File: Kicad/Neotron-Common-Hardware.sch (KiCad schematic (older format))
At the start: 12 parts

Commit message: Added empty SD card sheet.
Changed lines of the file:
@@
 $Descr A4 11693 8268
 encoding utf-8
-Sheet 1 9
+Sheet 1 10
 Title "Neotron Common Hardware"
 Date "2020-12-25"
@@
 NoConn ~ 4000 3250
 NoConn ~ 4000 3350
+$Sheet
+S 7000 3000 1000 1000
+U 5FEF6B08
+F0 "SD Card" 50
+F1 "sdcard.sch" 50
+$EndSheet
 $EndSCHEMATC

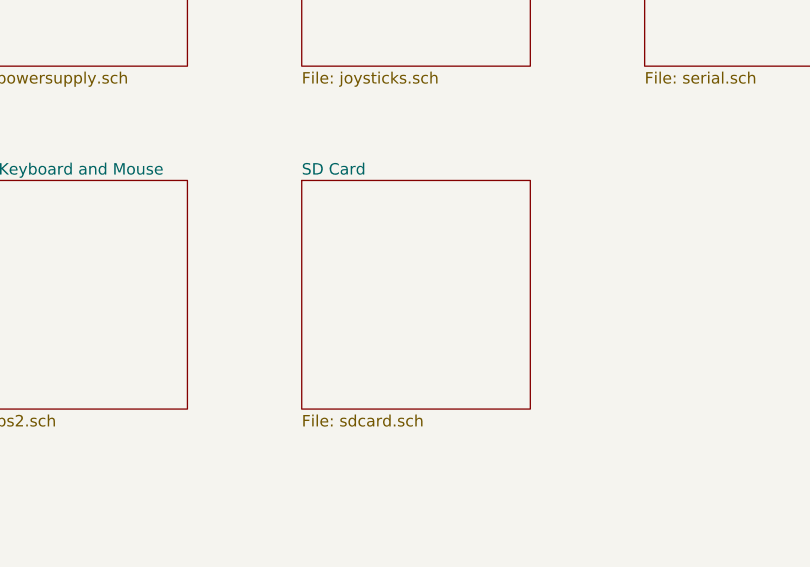
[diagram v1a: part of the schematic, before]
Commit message: Added SD card sheet.
Simple setup - 10k pullups, no ESD protection.
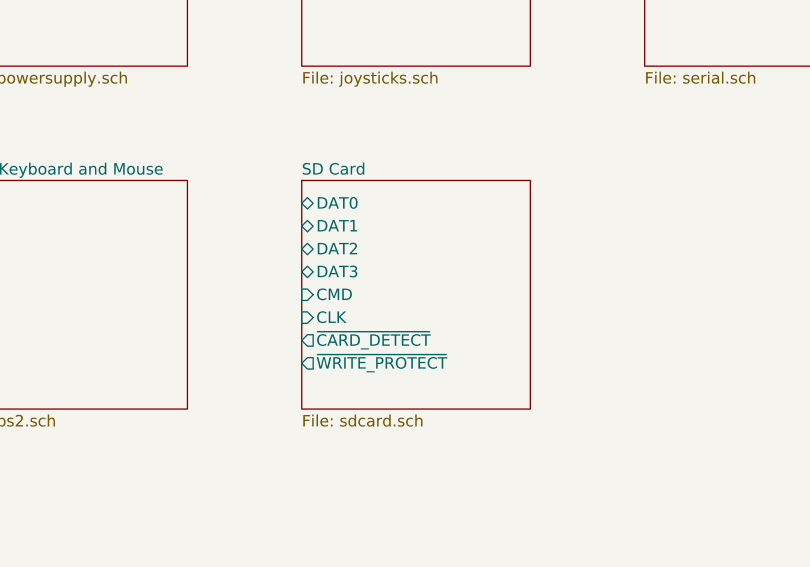
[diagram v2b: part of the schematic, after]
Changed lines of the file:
@@
 F0 "SD Card" 50
 F1 "sdcard.sch" 50
+F2 "DAT2" B L 7000 3300 50
+F3 "DAT3" B L 7000 3400 50
+F4 "CMD" I L 7000 3500 50
+F5 "CLK" I L 7000 3600 50
+F6 "DAT0" B L 7000 3100 50
+F7 "DAT1" B L 7000 3200 50
+F8 "~CARD_DETECT" O L 7000 3700 50
+F9 "~WRITE_PROTECT" O L 7000 3800 50
 $EndSheet
 $EndSCHEMATC

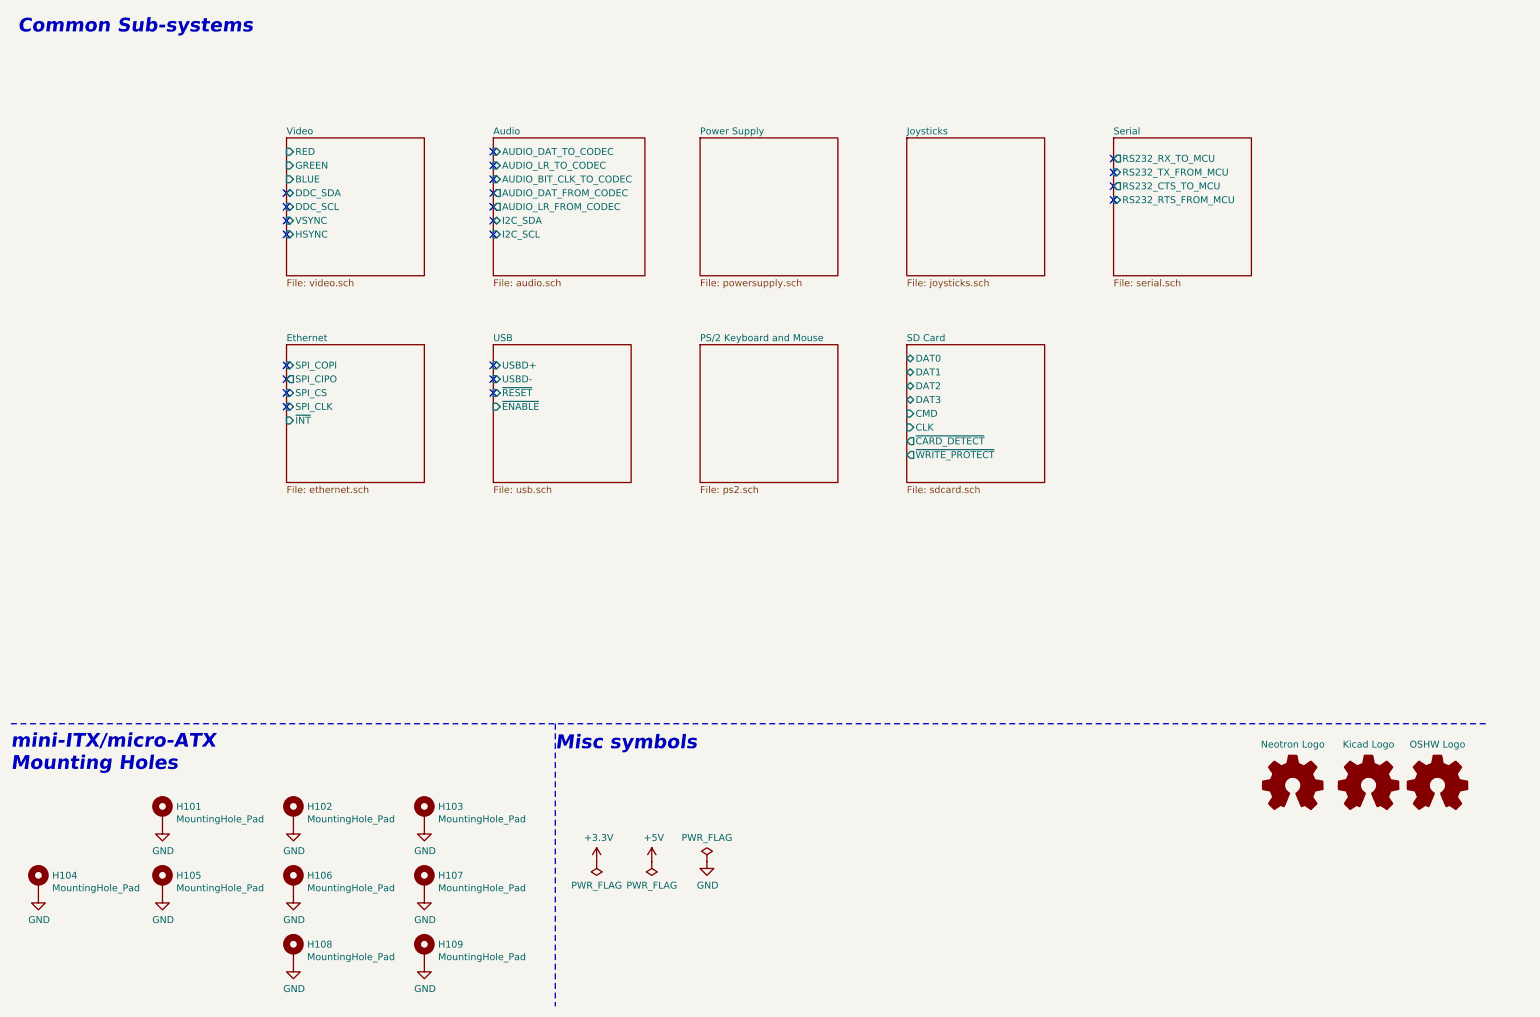
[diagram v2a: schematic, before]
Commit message: Completed PSU design.
Also changed footprint for stacked USB connector to change
shield pins from SHx to Pin 9.
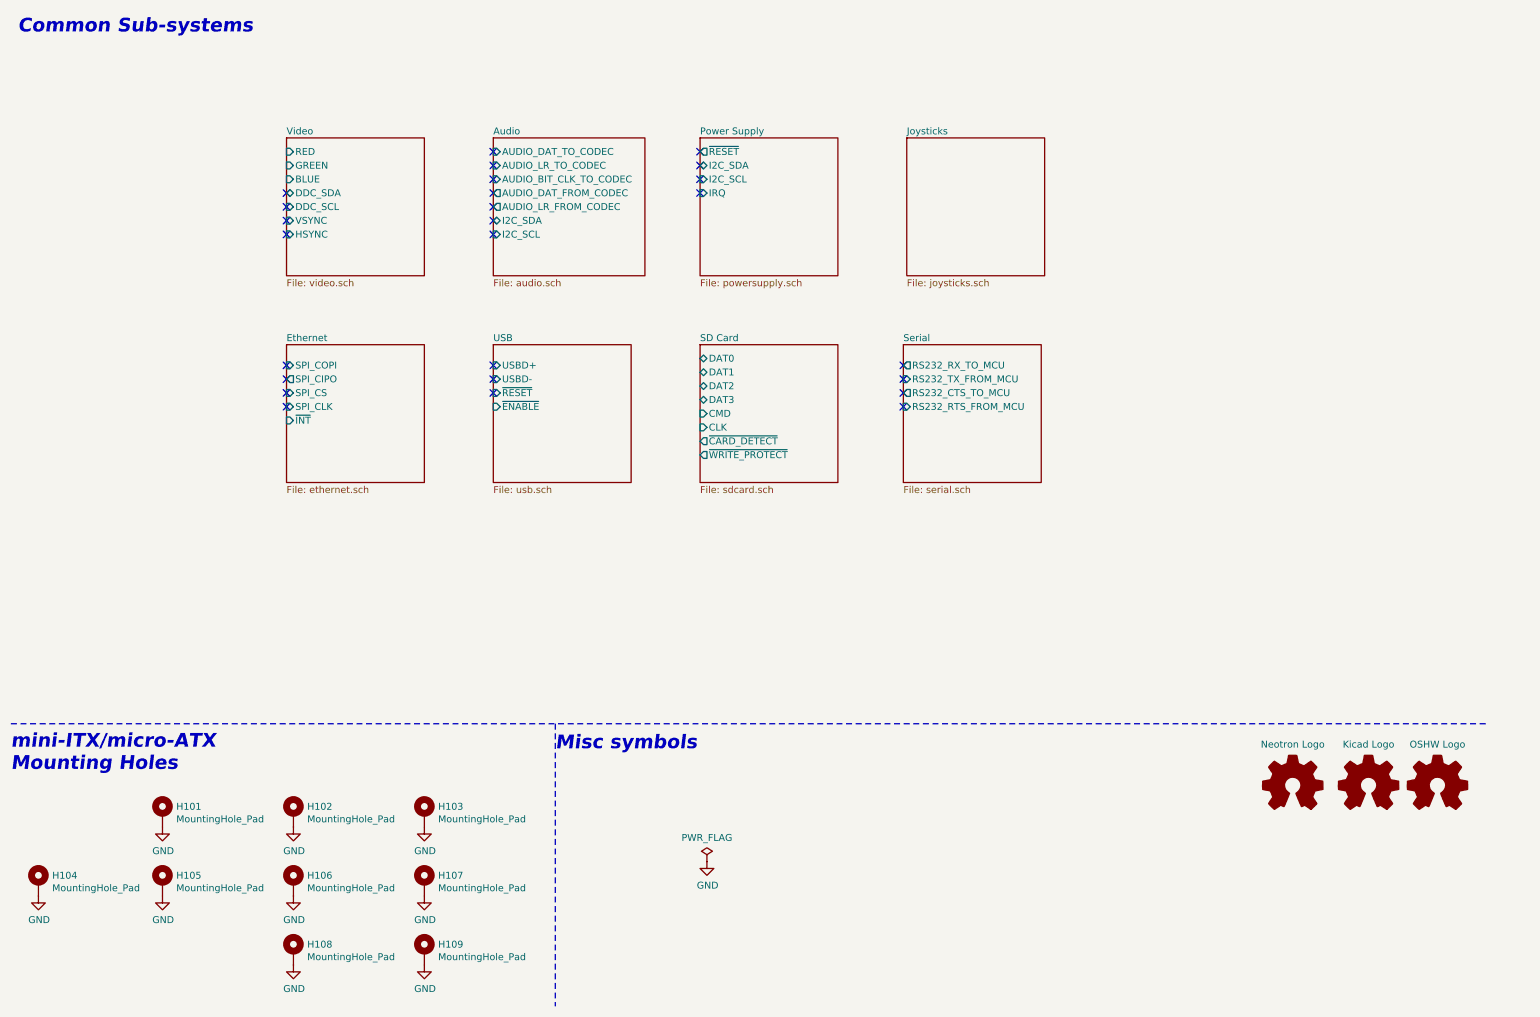
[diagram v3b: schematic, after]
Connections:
- no-connect marks 22 -> 26
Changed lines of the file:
@@
 $Descr A4 11693 8268
 encoding utf-8
-Sheet 1 10
+Sheet 1 9
 Title "Neotron Common Hardware"
-Date "2020-12-25"
+Date "2020-12-26"
 Rev "[Uncontrolled]"
 Comp "https://neotron-compute.github.io/"
@@
 F0 "Power Supply" 50
 F1 "powersupply.sch" 50
-$EndSheet
-$Sheet
-S 5500 3000 1000 1000
-U 5FDEDE75
-F0 "PS/2 Keyboard and Mouse" 50
-F1 "ps2.sch" 50
-$EndSheet
-$Sheet
-S 8500 1500 1000 1000
+F2 "~RESET" O L 5500 1600 50
+F3 "I2C_SDA" B L 5500 1700 50
+F4 "I2C_SCL" I L 5500 1800 50
+F5 "IRQ" I L 5500 1900 50
+$EndSheet
+$Sheet
+S 6975 3000 1000 1000
 U 5FDF53DB
 F0 "Serial" 50
 F1 "serial.sch" 50
-F2 "RS232_TX_FROM_MCU" I L 8500 1750 50
-F3 "RS232_RX_TO_MCU" O L 8500 1650 50
-F4 "RS232_RTS_FROM_MCU" I L 8500 1950 50
-F5 "RS232_CTS_TO_MCU" O L 8500 1850 50
+F2 "RS232_TX_FROM_MCU" I L 6975 3250 50
+F3 "RS232_RX_TO_MCU" O L 6975 3150 50
+F4 "RS232_RTS_FROM_MCU" I L 6975 3450 50
+F5 "RS232_CTS_TO_MCU" O L 6975 3350 50
 $EndSheet
 $Sheet
@@
 F1 "joysticks.sch" 50
 $EndSheet
-$Comp
-L power:+3.3V #PWR0101
-U 1 1 60A59BC0
-P 4750 6750
-F 0 "#PWR0101" H 4750 6600 50  0001 C CNN
-F 1 "+3.3V" H 4765 6923 50  0000 C CNN
-F 2 "" H 4750 6750 50  0001 C CNN
-F 3 "" H 4750 6750 50  0001 C CNN
-	1    4750 6750
-	1    0    0    -1
-$EndComp
-$Comp
-L power:+5V #PWR0102
-U 1 1 60A5A21B
-P 5150 6750
-F 0 "#PWR0102" H 5150 6600 50  0001 C CNN
-F 1 "+5V" H 5165 6923 50  0000 C CNN
-F 2 "" H 5150 6750 50  0001 C CNN
-F 3 "" H 5150 6750 50  0001 C CNN
-	1    5150 6750
-	1    0    0    -1
-$EndComp
-$Comp
-L power:PWR_FLAG #FLG0102
-U 1 1 60A5B443
-P 5150 6750
-F 0 "#FLG0102" H 5150 6825 50  0001 C CNN
-F 1 "PWR_FLAG" H 5150 6923 50  0000 C CNN
-F 2 "" H 5150 6750 50  0001 C CNN
-F 3 "~" H 5150 6750 50  0001 C CNN
-	1    5150 6750
-	-1   0    0    1
-$EndComp
-$Comp
-L power:PWR_FLAG #FLG0101
-U 1 1 60A5BC87
-P 4750 6750
-F 0 "#FLG0101" H 4750 6825 50  0001 C CNN
-F 1 "PWR_FLAG" H 4750 6923 50  0000 C CNN
-F 2 "" H 4750 6750 50  0001 C CNN
-F 3 "~" H 4750 6750 50  0001 C CNN
-	1    4750 6750
-	-1   0    0    1
-$EndComp
 NoConn ~ 4000 1600
 NoConn ~ 4000 1700
@@
 NoConn ~ 4000 2100
 NoConn ~ 4000 2200
-NoConn ~ 8500 1650
-NoConn ~ 8500 1750
-NoConn ~ 8500 1850
-NoConn ~ 8500 1950
+NoConn ~ 6975 3150
+NoConn ~ 6975 3250
+NoConn ~ 6975 3350
+NoConn ~ 6975 3450
 NoConn ~ 2500 3250
 NoConn ~ 2500 3350
@@
 NoConn ~ 2500 2100
 NoConn ~ 2500 2200
+NoConn ~ 4000 3150
+NoConn ~ 4000 3250
+NoConn ~ 4000 3350
+$Sheet
+S 5500 3000 1000 1000
+U 5FEF6B08
+F0 "SD Card" 50
+F1 "sdcard.sch" 50
+F2 "DAT2" B L 5500 3300 50
+F3 "DAT3" B L 5500 3400 50
+F4 "CMD" I L 5500 3500 50
+F5 "CLK" I L 5500 3600 50
+F6 "DAT0" B L 5500 3100 50
+F7 "DAT1" B L 5500 3200 50
+F8 "~CARD_DETECT" O L 5500 3700 50
+F9 "~WRITE_PROTECT" O L 5500 3800 50
+$EndSheet
+$Comp
+L power:PWR_FLAG #FLG0103
+U 1 1 60A5B22E
+P 5550 6750
+F 0 "#FLG0103" H 5550 6825 50  0001 C CNN
+F 1 "PWR_FLAG" H 5550 6923 50  0000 C CNN
+F 2 "" H 5550 6750 50  0001 C CNN
+F 3 "~" H 5550 6750 50  0001 C CNN
+	1    5550 6750
+	1    0    0    -1
+$EndComp
 $Comp
 L power:GND #PWR0103
@@
 	1    0    0    -1
 $EndComp
-$Comp
-L power:PWR_FLAG #FLG0103
-U 1 1 60A5B22E
-P 5550 6750
-F 0 "#FLG0103" H 5550 6825 50  0001 C CNN
-F 1 "PWR_FLAG" H 5550 6923 50  0000 C CNN
-F 2 "" H 5550 6750 50  0001 C CNN
-F 3 "~" H 5550 6750 50  0001 C CNN
-	1    5550 6750
-	1    0    0    -1
-$EndComp
-NoConn ~ 4000 3150
-NoConn ~ 4000 3250
-NoConn ~ 4000 3350
-$Sheet
-S 7000 3000 1000 1000
-U 5FEF6B08
-F0 "SD Card" 50
-F1 "sdcard.sch" 50
-F2 "DAT2" B L 7000 3300 50
-F3 "DAT3" B L 7000 3400 50
-F4 "CMD" I L 7000 3500 50
-F5 "CLK" I L 7000 3600 50
-F6 "DAT0" B L 7000 3100 50
-F7 "DAT1" B L 7000 3200 50
-F8 "~CARD_DETECT" O L 7000 3700 50
-F9 "~WRITE_PROTECT" O L 7000 3800 50
-$EndSheet
+NoConn ~ 5500 1600
+NoConn ~ 5500 1700
+NoConn ~ 5500 1800
+NoConn ~ 5500 1900
 $EndSCHEMATC

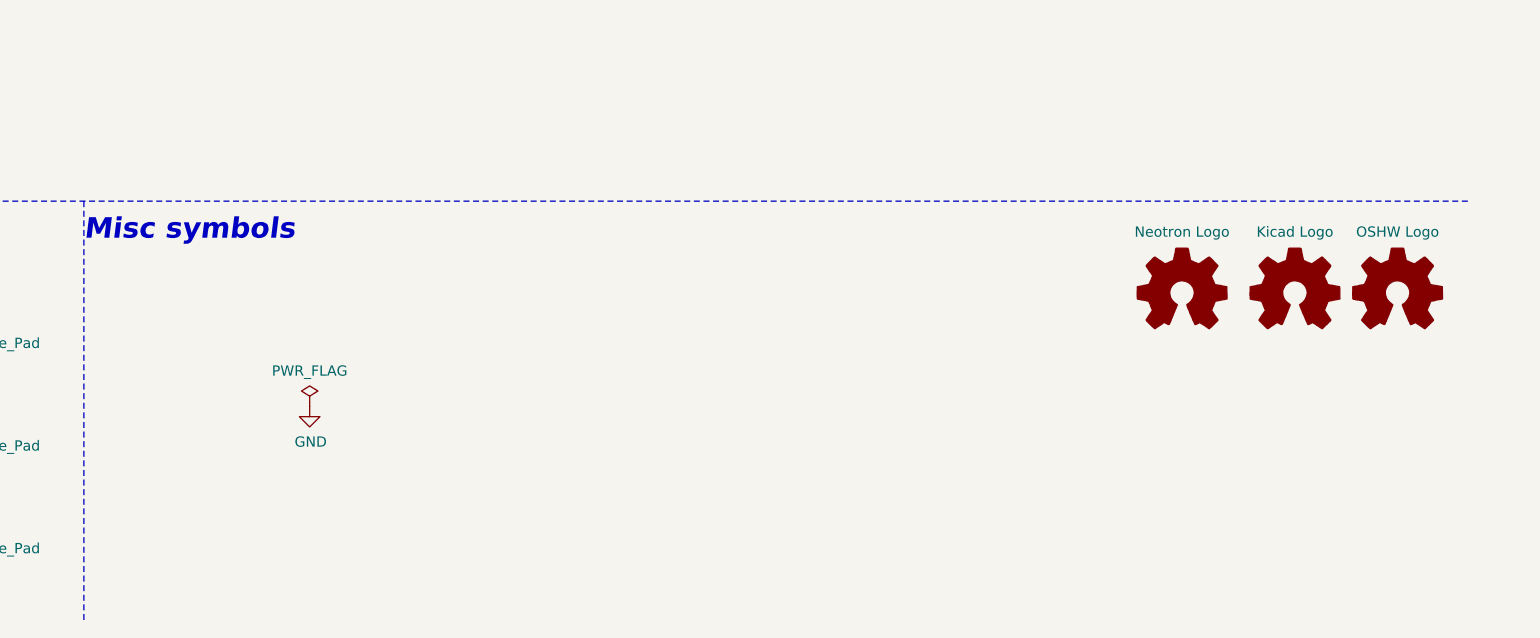
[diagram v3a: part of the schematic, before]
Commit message: Replaced NUC029 (TSSOP) with KE04 (SOIC).
Also updated the BOM with some part nos.
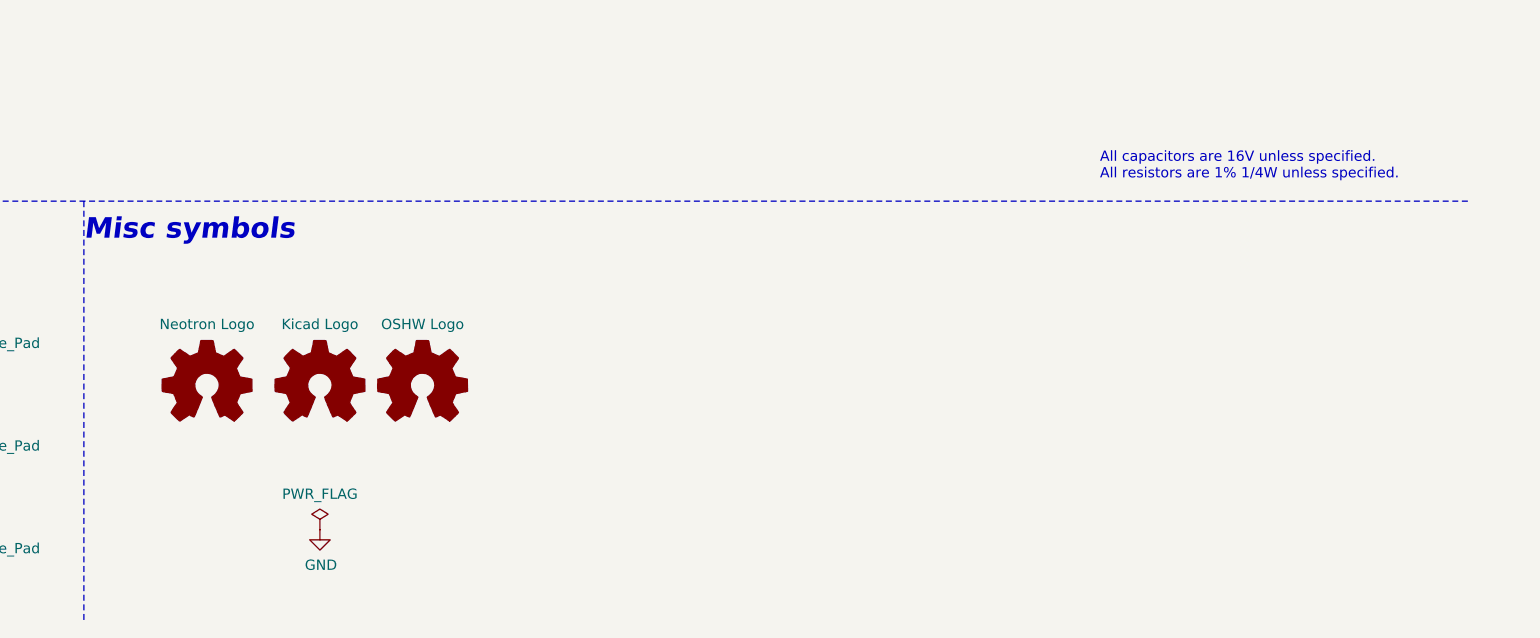
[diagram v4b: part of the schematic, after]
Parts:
- H101, H102, H103, H104, H105, H106, H107, H108, H109, LOGO101, LOGO102, LOGO103: DNP (none) -> 0
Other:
- note added: "All capacitors are 16V unless specified.\nAll resistors are 1% 1/4W unless specified."
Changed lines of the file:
@@
 F 2 "MountingHole:MountingHole_4.3mm_M4_Pad_Via" H 1600 6400 50  0001 C CNN
 F 3 "~" H 1600 6400 50  0001 C CNN
+F 4 "0" H 1600 6400 50  0001 C CNN "DNP"
 	1    1600 6400
 	1    0    0    -1
@@
 F 2 "MountingHole:MountingHole_4.3mm_M4_Pad_Via" H 1600 6900 50  0001 C CNN
 F 3 "~" H 1600 6900 50  0001 C CNN
+F 4 "0" H 1600 6900 50  0001 C CNN "DNP"
 	1    1600 6900
 	1    0    0    -1
@@
 F 2 "MountingHole:MountingHole_4.3mm_M4_Pad_Via" H 2550 6400 50  0001 C CNN
 F 3 "~" H 2550 6400 50  0001 C CNN
+F 4 "0" H 2550 6400 50  0001 C CNN "DNP"
 	1    2550 6400
 	1    0    0    -1
@@
 F 2 "MountingHole:MountingHole_4.3mm_M4_Pad_Via" H 2550 6900 50  0001 C CNN
 F 3 "~" H 2550 6900 50  0001 C CNN
+F 4 "0" H 2550 6900 50  0001 C CNN "DNP"
 	1    2550 6900
 	1    0    0    -1
@@
 F 2 "MountingHole:MountingHole_4.3mm_M4_Pad_Via" H 3500 6400 50  0001 C CNN
 F 3 "~" H 3500 6400 50  0001 C CNN
+F 4 "0" H 3500 6400 50  0001 C CNN "DNP"
 	1    3500 6400
 	1    0    0    -1
@@
 F 2 "MountingHole:MountingHole_4.3mm_M4_Pad_Via" H 2550 7400 50  0001 C CNN
 F 3 "~" H 2550 7400 50  0001 C CNN
+F 4 "0" H 2550 7400 50  0001 C CNN "DNP"
 	1    2550 7400
 	1    0    0    -1
@@
 F 2 "MountingHole:MountingHole_4.3mm_M4_Pad_Via" H 700 6900 50  0001 C CNN
 F 3 "~" H 700 6900 50  0001 C CNN
+F 4 "0" H 700 6900 50  0001 C CNN "DNP"
 	1    700  6900
 	1    0    0    -1
@@
 F 2 "MountingHole:MountingHole_4.3mm_M4_Pad_Via" H 3500 7400 50  0001 C CNN
 F 3 "~" H 3500 7400 50  0001 C CNN
+F 4 "0" H 3500 7400 50  0001 C CNN "DNP"
 	1    3500 7400
 	1    0    0    -1
@@
 F 2 "MountingHole:MountingHole_4.3mm_M4_Pad_Via" H 3500 6900 50  0001 C CNN
 F 3 "~" H 3500 6900 50  0001 C CNN
+F 4 "0" H 3500 6900 50  0001 C CNN "DNP"
 	1    3500 6900
 	1    0    0    -1
@@
 L Graphic:Logo_Open_Hardware_Small LOGO101
 U 1 1 5FE3E77B
-P 10850 6200
-F 0 "LOGO101" H 10850 6475 50  0001 C CNN
-F 1 "OSHW Logo" H 10850 6500 50  0000 C CNN
-F 2 "Symbol:OSHW-Logo_11.4x12mm_SilkScreen" H 10850 6494 50  0001 C CNN
-F 3 "~" H 10850 6200 50  0001 C CNN
-	1    10850 6200
+P 6100 6650
+F 0 "LOGO101" H 6100 6925 50  0001 C CNN
+F 1 "OSHW Logo" H 6100 6950 50  0000 C CNN
+F 2 "Symbol:OSHW-Logo_11.4x12mm_SilkScreen" H 6100 6944 50  0001 C CNN
+F 3 "~" H 6100 6650 50  0001 C CNN
+F 4 "0" H 6100 6650 50  0001 C CNN "DNP"
+	1    6100 6650
 	1    0    0    -1
 $EndComp
@@
 L Graphic:Logo_Open_Hardware_Small LOGO102
 U 1 1 5FE412EB
-P 10350 6200
-F 0 "LOGO102" H 10350 6475 50  0001 C CNN
-F 1 "Kicad Logo" H 10350 6500 50  0000 C CNN
-F 2 "Symbol:KiCad-Logo2_12mm_SilkScreen" H 10350 6494 50  0001 C CNN
-F 3 "~" H 10350 6200 50  0001 C CNN
-	1    10350 6200
+P 5600 6650
+F 0 "LOGO102" H 5600 6925 50  0001 C CNN
+F 1 "Kicad Logo" H 5600 6950 50  0000 C CNN
+F 2 "Symbol:KiCad-Logo2_12mm_SilkScreen" H 5600 6944 50  0001 C CNN
+F 3 "~" H 5600 6650 50  0001 C CNN
+F 4 "0" H 5600 6650 50  0001 C CNN "DNP"
+	1    5600 6650
 	1    0    0    -1
 $EndComp
@@
 L Graphic:Logo_Open_Hardware_Small LOGO103
 U 1 1 5FE4193F
-P 9800 6200
-F 0 "LOGO103" H 9800 6475 50  0001 C CNN
-F 1 "Neotron Logo" H 9800 6500 50  0000 C CNN
-F 2 "Neotron-Common-Hardware:logo" H 9800 6494 50  0001 C CNN
-F 3 "~" H 9800 6200 50  0001 C CNN
-	1    9800 6200
+P 5050 6650
+F 0 "LOGO103" H 5050 6925 50  0001 C CNN
+F 1 "Neotron Logo" H 5050 6950 50  0000 C CNN
+F 2 "Neotron-Common-Hardware:logo" H 5050 6944 50  0001 C CNN
+F 3 "~" H 5050 6650 50  0001 C CNN
+F 4 "0" H 5050 6650 50  0001 C CNN "DNP"
+	1    5050 6650
 	1    0    0    -1
 $EndComp
@@
 L power:PWR_FLAG #FLG0103
 U 1 1 60A5B22E
-P 5550 6750
-F 0 "#FLG0103" H 5550 6825 50  0001 C CNN
-F 1 "PWR_FLAG" H 5550 6923 50  0000 C CNN
-F 2 "" H 5550 6750 50  0001 C CNN
-F 3 "~" H 5550 6750 50  0001 C CNN
-	1    5550 6750
+P 5600 7350
+F 0 "#FLG0103" H 5600 7425 50  0001 C CNN
+F 1 "PWR_FLAG" H 5600 7523 50  0000 C CNN
+F 2 "" H 5600 7350 50  0001 C CNN
+F 3 "~" H 5600 7350 50  0001 C CNN
+	1    5600 7350
 	1    0    0    -1
 $EndComp
@@
 L power:GND #PWR0103
 U 1 1 60A5AA95
-P 5550 6750
-F 0 "#PWR0103" H 5550 6500 50  0001 C CNN
-F 1 "GND" H 5555 6577 50  0000 C CNN
-F 2 "" H 5550 6750 50  0001 C CNN
-F 3 "" H 5550 6750 50  0001 C CNN
-	1    5550 6750
+P 5600 7350
+F 0 "#PWR0103" H 5600 7100 50  0001 C CNN
+F 1 "GND" H 5605 7177 50  0000 C CNN
+F 2 "" H 5600 7350 50  0001 C CNN
+F 3 "" H 5600 7350 50  0001 C CNN
+	1    5600 7350
 	1    0    0    -1
 $EndComp
@@
 NoConn ~ 5500 1800
 NoConn ~ 5500 1900
+Text Notes 9400 5650 0    50   ~ 0
+All capacitors are 16V unless specified.\nAll resistors are 1% 1/4W unless specified.
 $EndSCHEMATC
